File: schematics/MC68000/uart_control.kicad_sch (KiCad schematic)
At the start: 4 parts, among them J11 Conn_02x20_Counter_Clockwise, J12 Conn_02x37_Row_Letter_Last, U28 74LS139, U29 74LS138

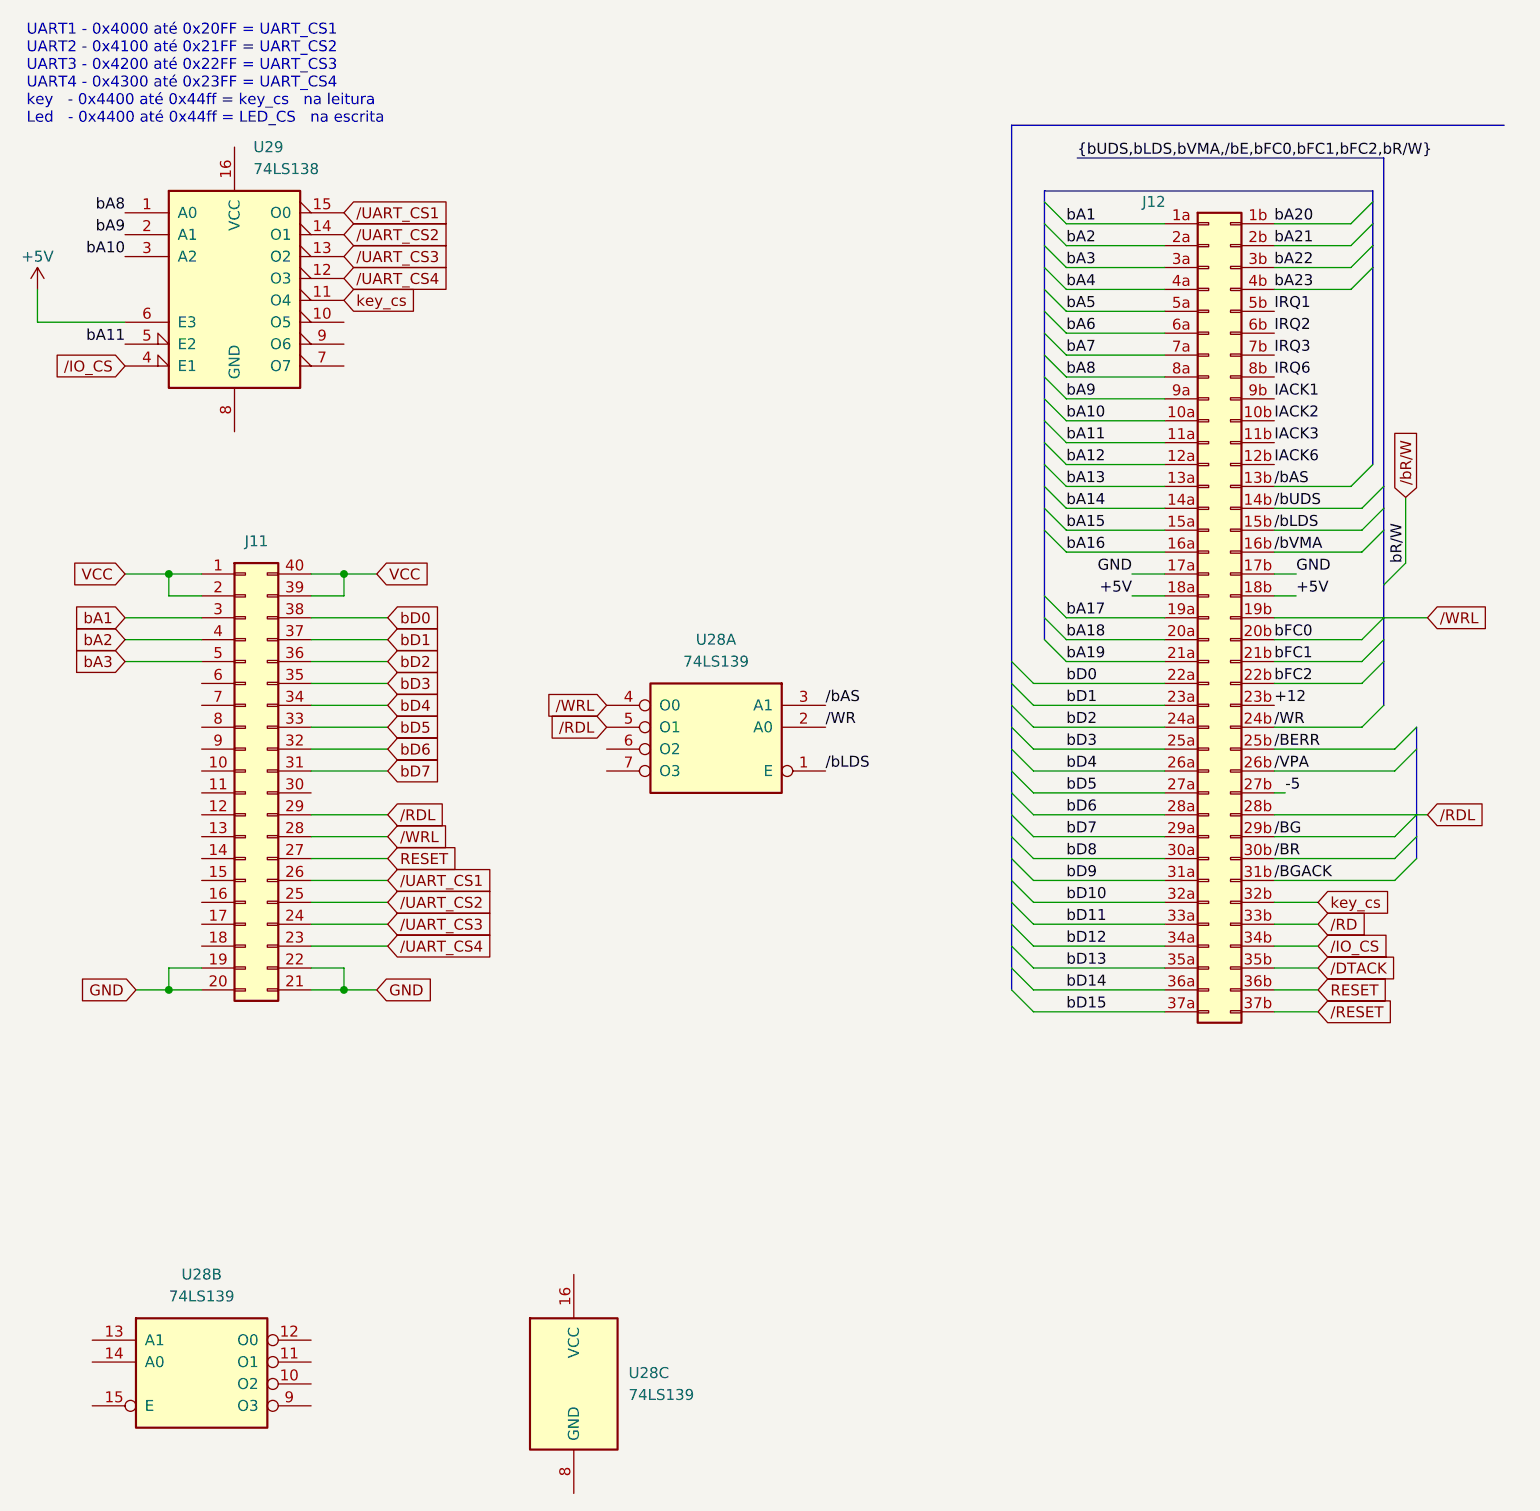
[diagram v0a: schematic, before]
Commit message: Added ch376s
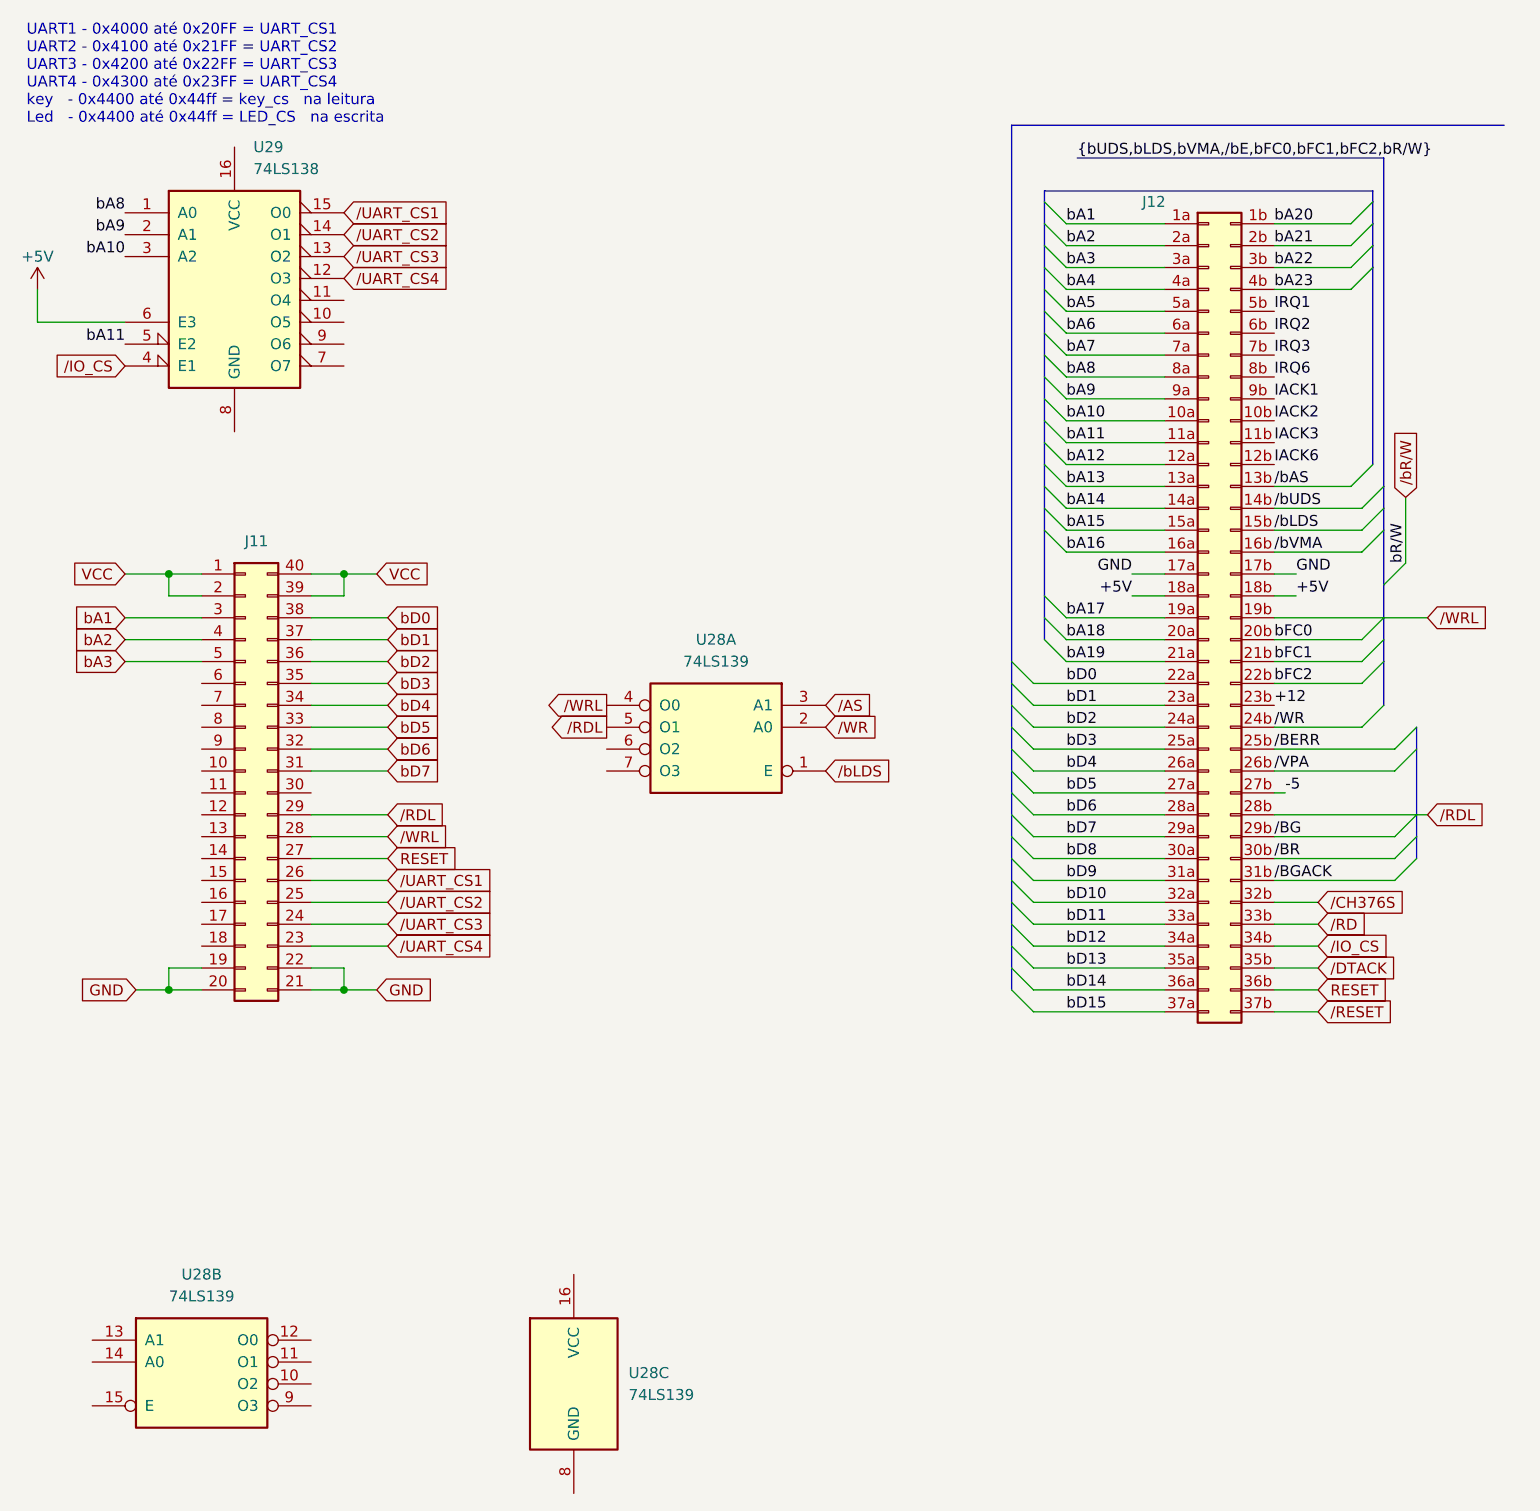
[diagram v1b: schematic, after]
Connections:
- net /bAS: no longer U28.3 (A1)
- net key_cs: no longer names the net of U29.11 (O4)
- net key_cs: no longer J12.32b (Pin_32b)
- new net /AS: U28.3 (A1)
- new net /CH376S: J12.32b (Pin_32b)
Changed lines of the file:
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@@
+	(wire
+		(pts
+			(xy 60.96 113.03) (xy 52.07 113.03)
+		)
+		(stroke
+			(width 0)
+			(type default)
+		)
+	)
+	(wire
+		(pts
+			(xy 139.7 62.23) (xy 151.13 62.23)
+		)
+		(stroke
+			(width 0)
+			(type default)
+		)
+	)
+	(wire
+		(pts
+			(xy 60.96 118.11) (xy 52.07 118.11)
+		)
+		(stroke
+			(width 0)
+			(type default)
+		)
+	)
 	(wire
 		(pts
 			(xy 168.91 120.65) (xy 163.83 120.65)
-		)
-		(stroke
-			(width 0)
-			(type default)
-		)
-	)
-	(wire
-		(pts
-			(xy 60.96 113.03) (xy 52.07 113.03)
-		)
-		(stroke
-			(width 0)
-			(type default)
-		)
-	)
-	(wire
-		(pts
-			(xy 139.7 62.23) (xy 151.13 62.23)
-		)
-		(stroke
-			(width 0)
-			(type default)
-		)
-	)
-	(wire
-		(pts
-			(xy 60.96 118.11) (xy 52.07 118.11)
 		)
 		(stroke
@@
 		)
 	)
-	(label "{slash}WR"
-		(at 111.76 100.33 0)
-		(effects
-			(font
-				(size 1.27 1.27)
-			)
-			(justify left bottom)
-		)
-	)
 	(label "+5V"
 		(at 147.32 85.09 180)
@@
 		)
 	)
-	(label "{slash}bLDS"
-		(at 111.76 105.41 0)
-		(effects
-			(font
-				(size 1.27 1.27)
-			)
-			(justify left bottom)
-		)
-	)
 	(label "bA1"
 		(at 139.7 41.91 0)
@@
 		)
 	)
-	(label "{slash}bAS"
-		(at 111.76 97.79 0)
-		(effects
-			(font
-				(size 1.27 1.27)
-			)
-			(justify left bottom)
-		)
-	)
 	(label "bA2"
 		(at 139.7 44.45 0)
@@
 		)
 	)
-	(global_label "key_cs"
-		(shape input)
-		(at 55.88 50.8 0)
-		(fields_autoplaced yes)
-		(effects
-			(font
-				(size 1.27 1.27)
-			)
-			(justify left)
-		)
-		(property "Intersheetrefs" "${INTERSHEET_REFS}"
-			(at 65.0338 50.8 0)
-			(effects
-				(font
-					(size 1.27 1.27)
-				)
-				(justify left)
-				(hide yes)
-			)
-		)
-	)
 	(global_label "bD1"
 		(shape input)
@@
 	)
 	(global_label "{slash}RDL"
-		(shape input)
+		(shape output)
 		(at 86.36 100.33 180)
 		(fields_autoplaced yes)
@@
 		)
 	)
+	(global_label "{slash}WR"
+		(shape input)
+		(at 111.76 100.33 0)
+		(fields_autoplaced yes)
+		(effects
+			(font
+				(size 1.27 1.27)
+			)
+			(justify left)
+		)
+		(property "Intersheetrefs" "${INTERSHEET_REFS}"
+			(at 118.7971 100.33 0)
+			(effects
+				(font
+					(size 1.27 1.27)
+				)
+				(justify left)
+				(hide yes)
+			)
+		)
+	)
 	(global_label "{slash}UART_CS1"
 		(shape input)
@@
 		)
 	)
+	(global_label "{slash}AS"
+		(shape input)
+		(at 111.76 97.79 0)
+		(fields_autoplaced yes)
+		(effects
+			(font
+				(size 1.27 1.27)
+			)
+			(justify left)
+		)
+		(property "Intersheetrefs" "${INTERSHEET_REFS}"
+			(at 118.3738 97.79 0)
+			(effects
+				(font
+					(size 1.27 1.27)
+				)
+				(justify left)
+				(hide yes)
+			)
+		)
+	)
 	(global_label "bD0"
 		(shape input)
@@
 		)
 	)
+	(global_label "{slash}CH376S"
+		(shape input)
+		(at 168.91 120.65 0)
+		(fields_autoplaced yes)
+		(effects
+			(font
+				(size 1.27 1.27)
+			)
+			(justify left)
+		)
+		(property "Intersheetrefs" "${INTERSHEET_REFS}"
+			(at 180.6642 120.65 0)
+			(effects
+				(font
+					(size 1.27 1.27)
+				)
+				(justify left)
+				(hide yes)
+			)
+		)
+	)
 	(global_label "GND"
 		(shape input)
@@
 		)
 	)
+	(global_label "{slash}bLDS"
+		(shape input)
+		(at 111.76 105.41 0)
+		(fields_autoplaced yes)
+		(effects
+			(font
+				(size 1.27 1.27)
+			)
+			(justify left)
+		)
+		(property "Intersheetrefs" "${INTERSHEET_REFS}"
+			(at 120.7323 105.41 0)
+			(effects
+				(font
+					(size 1.27 1.27)
+				)
+				(justify left)
+				(hide yes)
+			)
+		)
+	)
 	(global_label "{slash}RDL"
 		(shape input)
@@
 	)
 	(global_label "{slash}WRL"
-		(shape input)
+		(shape output)
 		(at 86.36 97.79 180)
 		(fields_autoplaced yes)
@@
 				(hide yes)
 			)
-		)
-	)
-	(global_label "key_cs"
-		(shape input)
-		(at 168.91 120.65 0)
-		(fields_autoplaced yes)
-		(effects
-			(font
-				(size 1.27 1.27)
-			)
-			(justify left)
-		)
-		(property "Intersheetrefs" "${INTERSHEET_REFS}"
-			(at 178.0638 120.65 0)
-			(effects
-				(font
-					(size 1.27 1.27)
-				)
-				(justify left)
-				(hide yes)
-			)
